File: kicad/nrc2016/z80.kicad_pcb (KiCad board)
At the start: 2 copper layers, 104.8 x 111.8 mm, 37 parts, among them P2 CONN_01X02, P3 Jumper, SW1 RESET, U1 Z80CPU, U2 DIP_OSCILLATOR, U3 ATF16V8CV

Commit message: Moved directory layout around to clean things up
.. for future work etc.
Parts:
- LOGO1: footprint ncr2016_logo:nrc2016_top_logo_1600 -> nrc2016_logo:nrc2016_top_logo_1600
- LOGO2: footprint ncr2016_logo:nrc2016_bottom_logo_600_v3 -> nrc2016_logo:nrc2016_bottom_logo_600_v3
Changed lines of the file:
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@@
       (net 2 GND))
   )
-  (module ncr2016_logo:nrc2016_top_logo_1600 (layer Top)
+  (module nrc2016_logo:nrc2016_top_logo_1600 (layer Top)
     (at 81.788 83.82 90)
     (fp_text reference LOGO1 (at 0 0 90) (layer F.SilkS) hide
@@
     )
   )
-  (module ncr2016_logo:nrc2016_bottom_logo_600_v3 (layer Bottom)
+  (module nrc2016_logo:nrc2016_bottom_logo_600_v3 (layer Bottom)
     (at 95.758 77.47 270)
     (fp_text reference LOGO2 (at 0 0 270) (layer B.SilkS) hide

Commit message: Fixed up project paths and pcb footprint path moves
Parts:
- LOGO2: footprint nrc2016_logo:nrc2016_bottom_logo_600_v3 -> nrc2016_logo:nrc2016_bottom_logo_600_v2

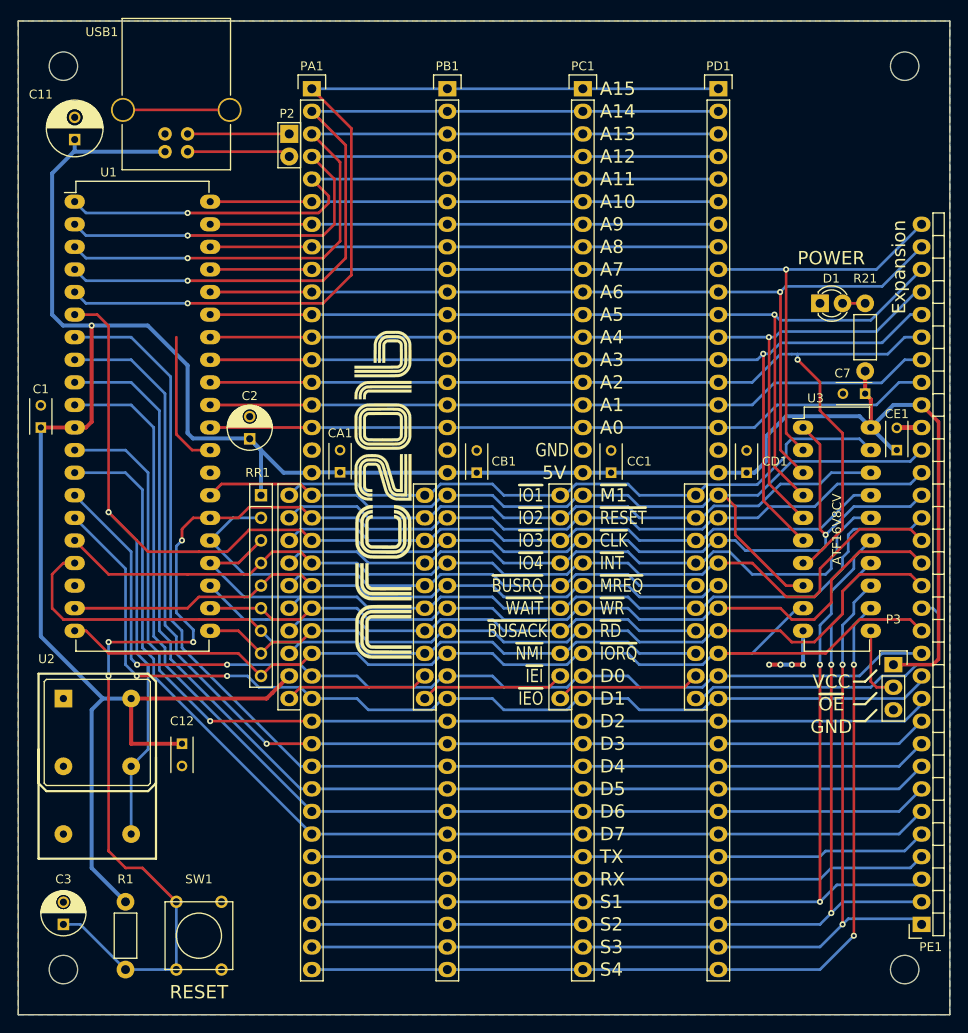
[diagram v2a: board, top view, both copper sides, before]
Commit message: Update nrc2016 schema and PCB to use new library symbols
I've added proper schematic symbols for the pre-defined bus sockets to
stop confusion and error by just using the generic "library" socket
component and then relying on the net names to define the pins. Screwed
me once with the VCC and GND switch around, not going to happen again.
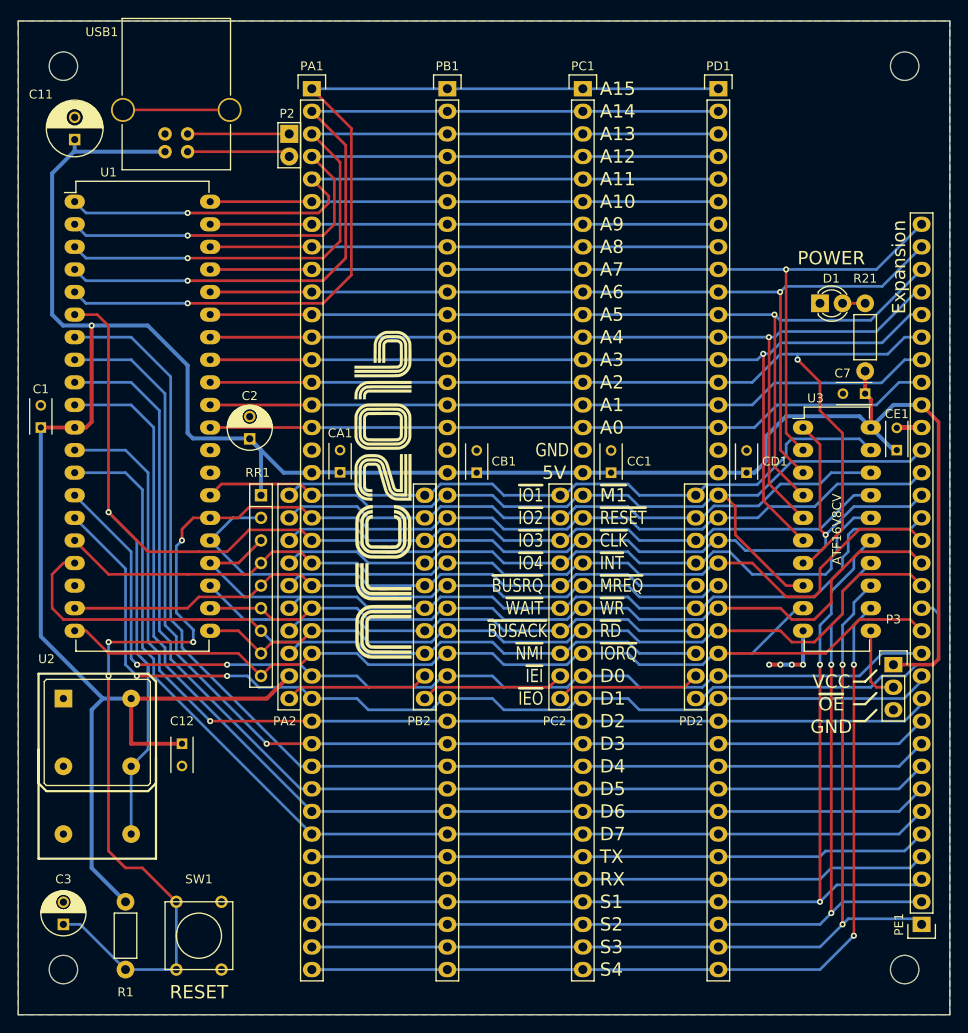
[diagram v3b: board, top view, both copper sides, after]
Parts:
- P2: value CONN_01X02 -> USB
- PA1, PB1, PC1, PD1: value CONN_01X40 -> Z80_BUS
- PA2, PB2, PC2, PD2: value CONN_01X10 -> IO_BUS
- PE1: value CONN_01X32 -> EXPANSION; footprint Socket_Strips:Socket_Strip_Angled_1x32 -> Socket_Strips:Socket_Strip_Straight_1x32
- moved R1 7.62 mm to (52.7, 137.2), turned to 90 degrees
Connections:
- R1 pad 1: VCC -> /~RESET
- R1 pad 2: /~RESET -> VCC
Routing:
- net GND: track 32.6 -> 17.1 mm

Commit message: More moving things around. Added sockets and pins symbols
Makes it easier for DRC and has hints for the right footprints already.
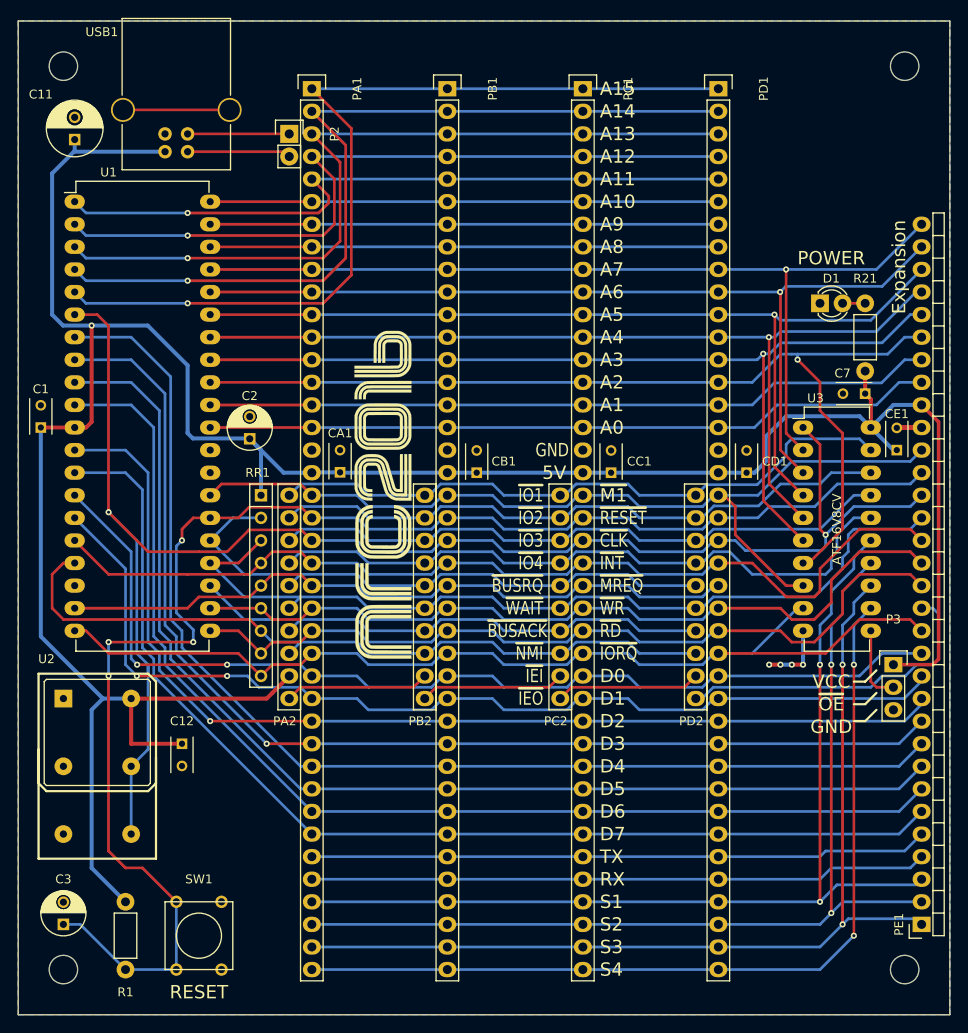
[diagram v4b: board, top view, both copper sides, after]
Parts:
- P2: value USB -> USB_SOCKET
- PA1, PB1, PC1, PD1: value Z80_BUS -> Z80_BUS_SOCKET
- PA2, PB2, PC2, PD2: value IO_BUS -> IO_BUS_SOCKET
- PE1: value EXPANSION -> EXPANSION_SOCKET; footprint Socket_Strips:Socket_Strip_Straight_1x32 -> Socket_Strip_Angled_1x32_nrc2016
